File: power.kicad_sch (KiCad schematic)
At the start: 22 parts, among them J15 Conn_01x04, U6 LMR51610XDBVR, U7 LM66100DCK, U8 LM66100DCK, U9 TLV74033PDBVR

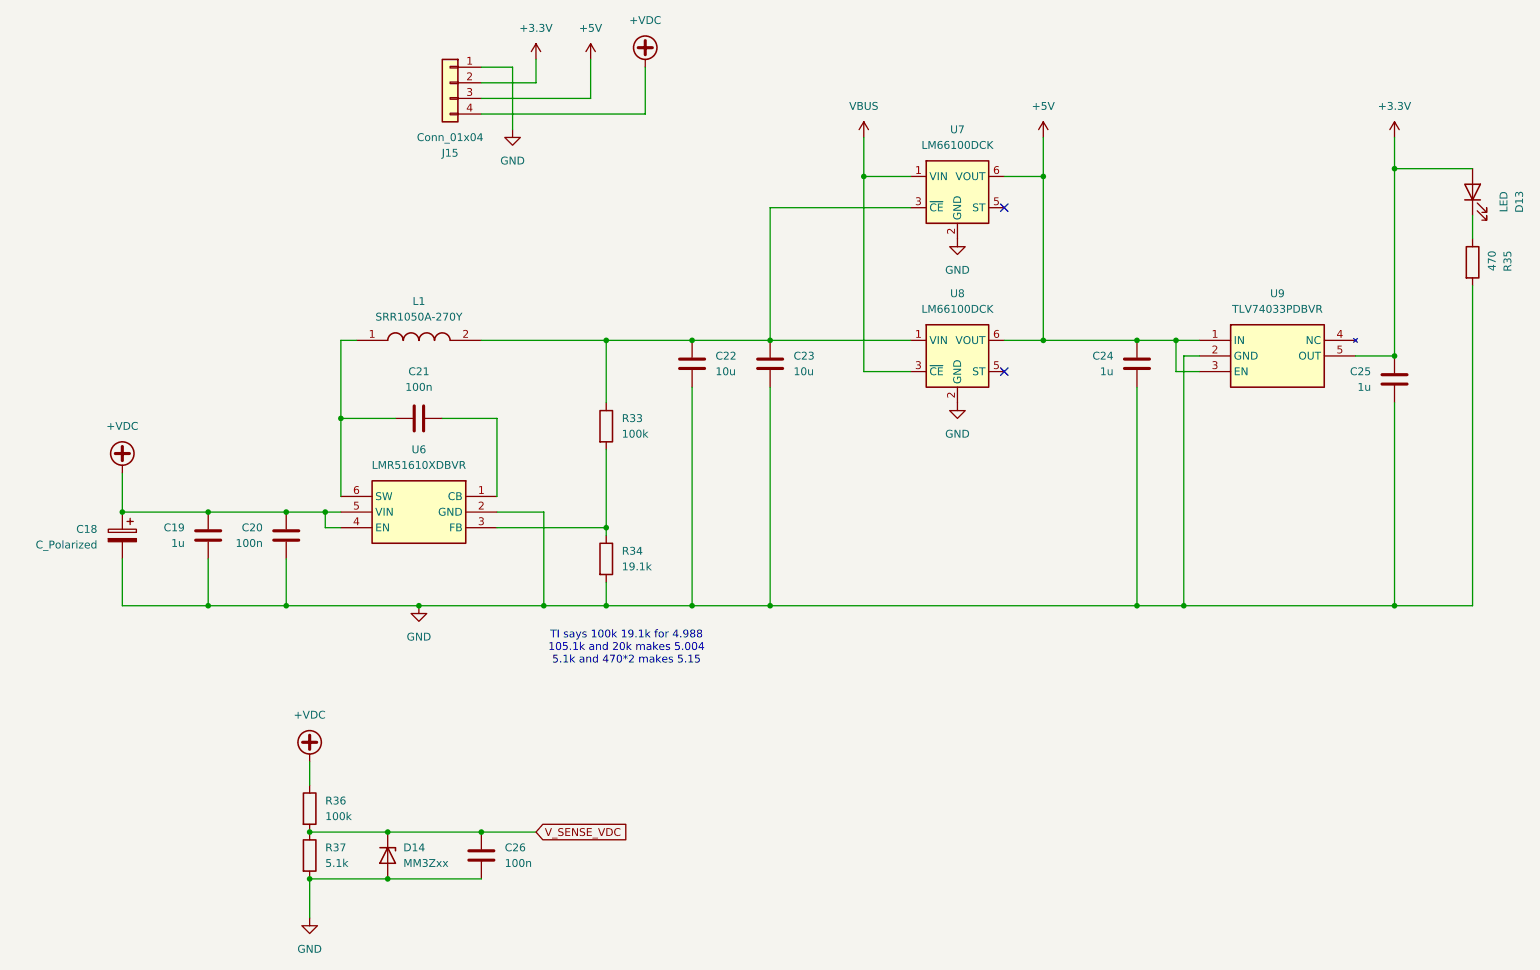
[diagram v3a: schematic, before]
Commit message: complete top layer layout
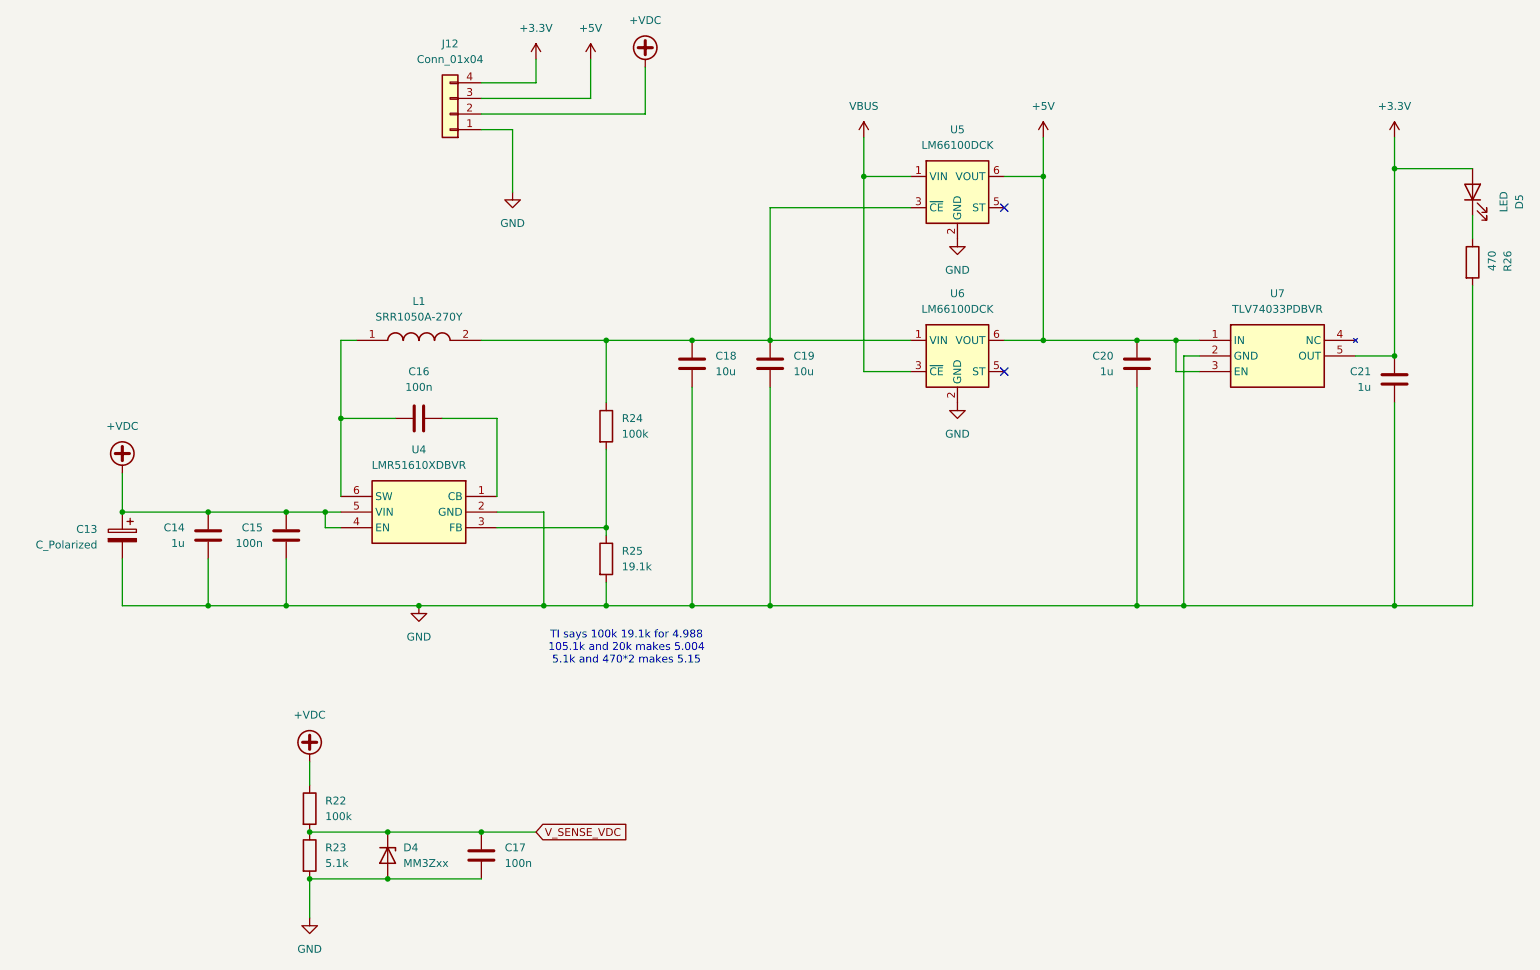
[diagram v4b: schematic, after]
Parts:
- renumbered C18 to C13, C19 to C14, C20 to C15, C21 to C16, C26 to C17, C22 to C18, C23 to C19, C24 to C20, C25 to C21, D14 to D4, D13 to D5, J15 to J12, R36 to R22, R37 to R23, R33 to R24, R34 to R25, R35 to R26, U6 to U4, U7 to U5, U8 to U6, U9 to U7
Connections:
- net +3.3V: now also J12.4 (Pin_4); no longer J12.2 (Pin_2)
- net +VDC: now also J12.2 (Pin_2); no longer J12.4 (Pin_4)
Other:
- moved on the sheet: J12

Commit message: complete layout, routing, and silkscreen
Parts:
- renumbered C13 to C12, C14 to C13, C15 to C14, C16 to C15, C17 to C16, C18 to C17, C19 to C18, C20 to C19, C21 to C20
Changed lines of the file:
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@@
 		(dnp no)
 		(fields_autoplaced yes)
-		(property "Reference" "C19"
+		(property "Reference" "C18"
 			(at 146.05 87.6299 0)
 			(effects
@@
 			(project ""
 				(path "/bd7590c0-6a37-4bf0-a9f2-f26180744ceb/497bfd7a-c06a-4d4d-a320-8405be197f02"
-					(reference "C19")
+					(reference "C18")
 					(unit 1)
 				)
@@
 		(on_board yes)
 		(dnp no)
-		(property "Reference" "C21"
+		(property "Reference" "C20"
 			(at 240.03 90.1699 0)
 			(effects
@@
 			(project "dmxdude"
 				(path "/bd7590c0-6a37-4bf0-a9f2-f26180744ceb/497bfd7a-c06a-4d4d-a320-8405be197f02"
-					(reference "C21")
+					(reference "C20")
 					(unit 1)
 				)
@@
 		(dnp no)
 		(fields_autoplaced yes)
-		(property "Reference" "C16"
+		(property "Reference" "C15"
 			(at 85.09 90.17 90)
 			(effects
@@
 			(project ""
 				(path "/bd7590c0-6a37-4bf0-a9f2-f26180744ceb/497bfd7a-c06a-4d4d-a320-8405be197f02"
-					(reference "C16")
+					(reference "C15")
 					(unit 1)
 				)
@@
 		(on_board yes)
 		(dnp no)
-		(property "Reference" "C15"
+		(property "Reference" "C14"
 			(at 59.69 115.5699 0)
 			(effects
@@
 			(project "dmxdude"
 				(path "/bd7590c0-6a37-4bf0-a9f2-f26180744ceb/497bfd7a-c06a-4d4d-a320-8405be197f02"
-					(reference "C15")
+					(reference "C14")
 					(unit 1)
 				)
@@
 		(dnp no)
 		(fields_autoplaced yes)
-		(property "Reference" "C17"
+		(property "Reference" "C16"
 			(at 99.06 167.6399 0)
 			(effects
@@
 			(project ""
 				(path "/bd7590c0-6a37-4bf0-a9f2-f26180744ceb/497bfd7a-c06a-4d4d-a320-8405be197f02"
-					(reference "C17")
+					(reference "C16")
 					(unit 1)
 				)
@@
 		(dnp no)
 		(fields_autoplaced yes)
-		(property "Reference" "C18"
+		(property "Reference" "C17"
 			(at 133.35 87.6299 0)
 			(effects
@@
 			(project ""
 				(path "/bd7590c0-6a37-4bf0-a9f2-f26180744ceb/497bfd7a-c06a-4d4d-a320-8405be197f02"
-					(reference "C18")
+					(reference "C17")
 					(unit 1)
 				)
@@
 		(on_board yes)
 		(dnp no)
-		(property "Reference" "C13"
+		(property "Reference" "C12"
 			(at 32.766 115.824 0)
 			(effects
@@
 			(project ""
 				(path "/bd7590c0-6a37-4bf0-a9f2-f26180744ceb/497bfd7a-c06a-4d4d-a320-8405be197f02"
-					(reference "C13")
+					(reference "C12")
 					(unit 1)
 				)
@@
 		(on_board yes)
 		(dnp no)
-		(property "Reference" "C20"
+		(property "Reference" "C19"
 			(at 198.12 87.6299 0)
 			(effects
@@
 			(project "dmxdude"
 				(path "/bd7590c0-6a37-4bf0-a9f2-f26180744ceb/497bfd7a-c06a-4d4d-a320-8405be197f02"
-					(reference "C20")
+					(reference "C19")
 					(unit 1)
 				)
@@
 		(on_board yes)
 		(dnp no)
-		(property "Reference" "C14"
+		(property "Reference" "C13"
 			(at 46.99 115.5699 0)
 			(effects
@@
 			(project "dmxdude"
 				(path "/bd7590c0-6a37-4bf0-a9f2-f26180744ceb/497bfd7a-c06a-4d4d-a320-8405be197f02"
-					(reference "C14")
-					(unit 1)
-				)
+					(reference "C13")
+					(unit 1)
+				)
